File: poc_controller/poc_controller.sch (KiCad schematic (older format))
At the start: 8 parts, among them J1 CONN_01X02, J2 CONN_01X06, U1 MIC5211, U2 dspic33EP128GP502, U3 dspic33EP128GP502, U4 MPC8025

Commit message: Schematic updates for POC controller.
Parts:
- removed U2, U3: dspic33EP128GP502, symbol dspic33EP128GP502
- added C3, C4, C5: 0.1uF, symbol C
- added C6: 10uF, symbol C
- added C? (x2): C, symbol C
- added C? (x5): 100nF, symbol CP1
- added C?: 1uF, symbol CP1
- added C?: CP1, symbol CP1
- added J?: CONN_01X06, symbol CONN_01X06
- added J? (x2): CONN_01X02, symbol CONN_01X02
- added R1: 47k, symbol R
- added R?: R, symbol R
- added R? (x3): 4.7k, symbol R
- added U? (x2): dsPIC33EPXXXMC502, symbol dsPIC33EPXXXMC502
- added U?: MAG3110, symbol MAG3110
- added U?: LSM6DS3H, symbol LSM6DS3H
- added Y1: Crystal, symbol Crystal
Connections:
- net labels added: CAN_RX, CAN_TX, CPU_MCLR, CPU_PGC, CPU_PGD, SCL, SDA
- wire segments 29 -> 98
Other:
- moved on the sheet: C1, C2

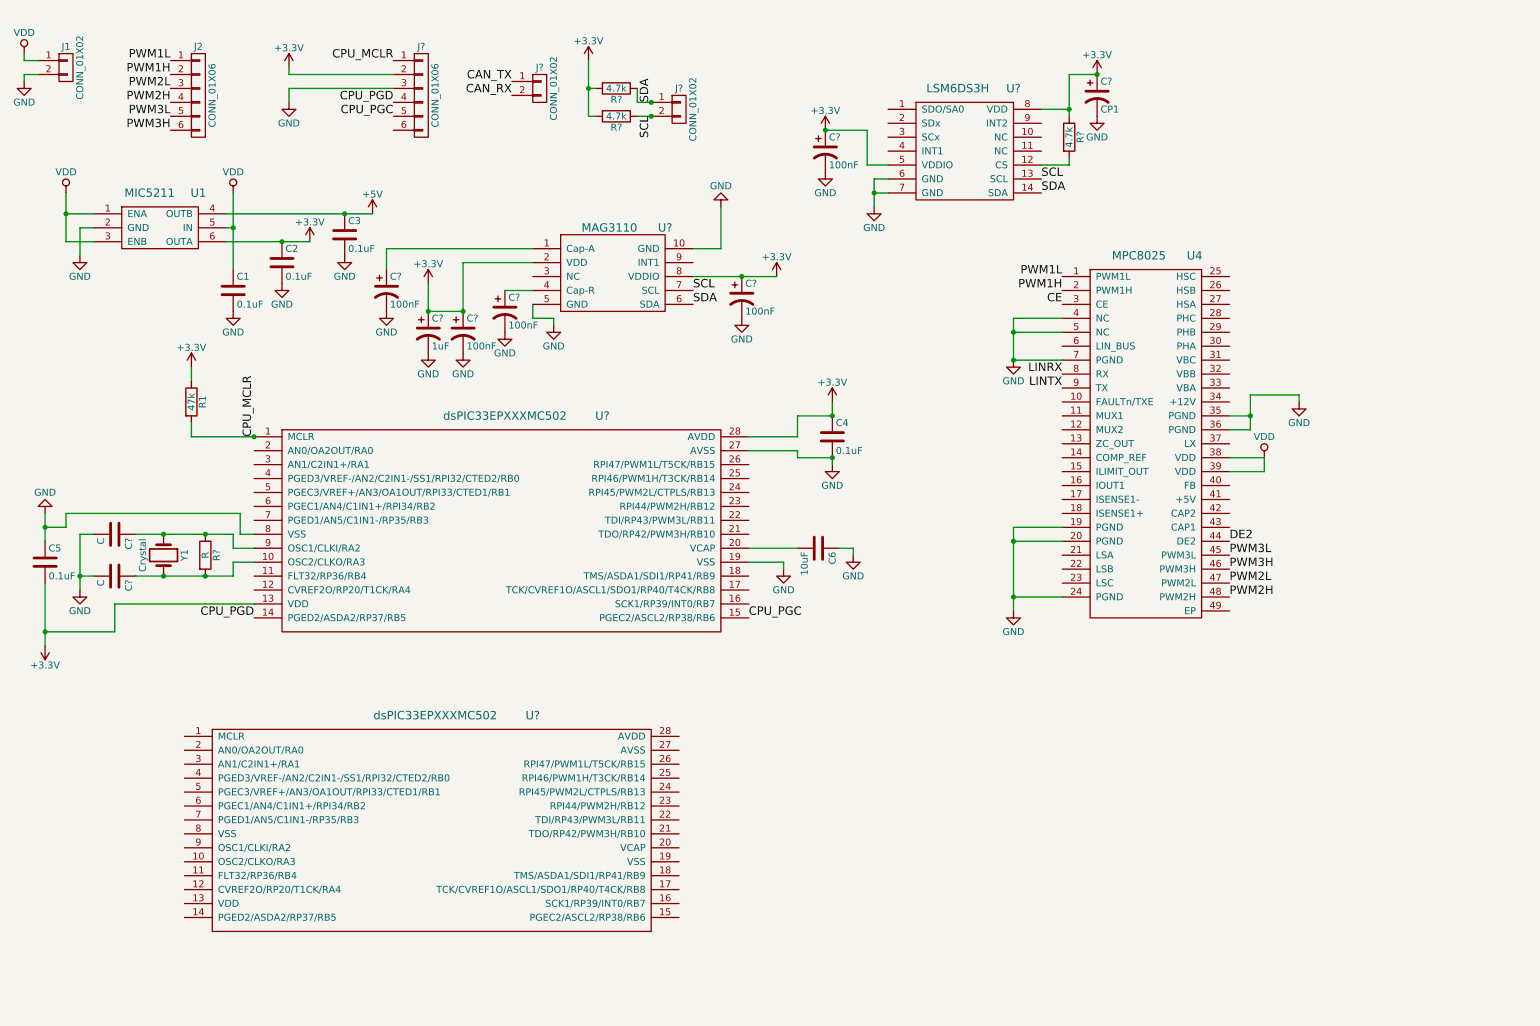
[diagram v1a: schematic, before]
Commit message: Start to break out sections into separate sheets.
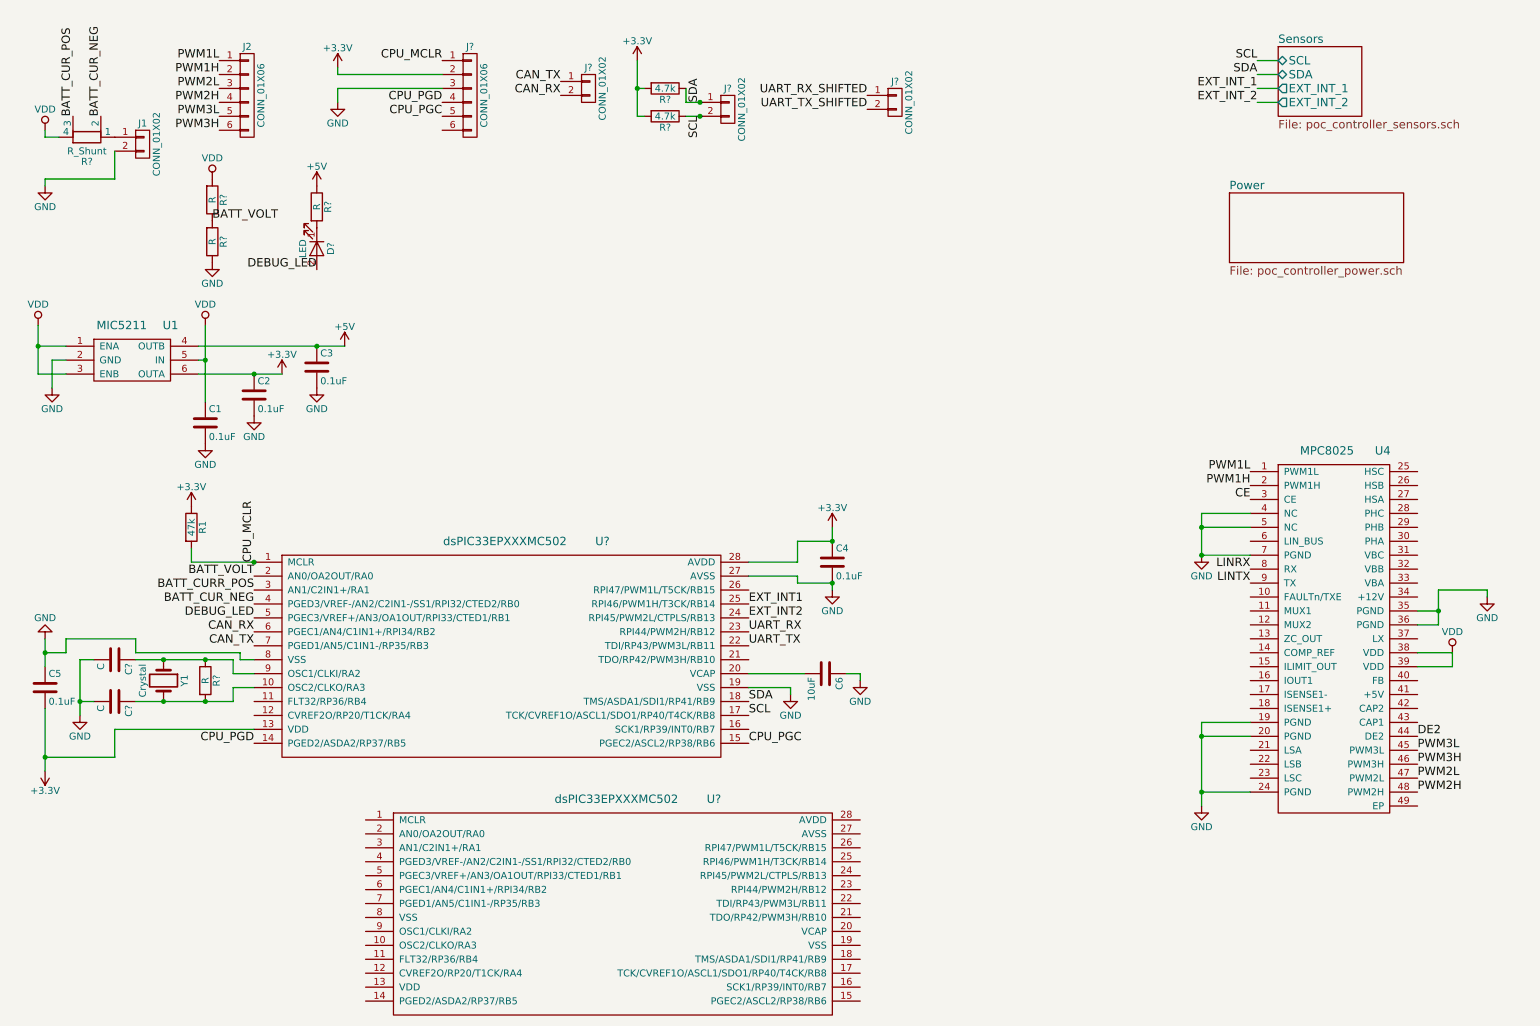
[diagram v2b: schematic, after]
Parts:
- removed C? (x5): 100nF, symbol CP1
- removed C?: 1uF, symbol CP1
- removed C?: CP1, symbol CP1
- removed R?: 4.7k, symbol R
- removed U?: MAG3110, symbol MAG3110
- removed U?: LSM6DS3H, symbol LSM6DS3H
- added D?: LED, symbol LED
- added J?: CONN_01X02, symbol CONN_01X02
- added R?: R_Shunt, symbol R_Shunt
- added R? (x3): R, symbol R
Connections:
- net +5V: now also R?.1
- net CAN_RX: now also U?.6 (PGEC1/AN4/C1IN1+/RPI34/RB2)
- net CAN_TX: now also U?.7 (PGED1/AN5/C1IN1-/RP35/RB3)
- net GND: now also R?.1
- net SCL: now also U?.17 (TCK/CVREF1O/ASCL1/SDO1/RP40/T4CK/RB8)
- net SDA: now also U?.18 (TMS/ASDA1/SDI1/RP41/RB9)
- net VDD: now also R?.2, R?.4; no longer J1.1 (P1)
- net BATT_VOLT: now reaches U?.2 (AN0/OA2OUT/RA0)
- net BATT_VOLT: now also R?.1, R?.2
- net UART_TX: now reaches U?.22 (TDI/RP43/PWM3L/RB11)
- net UART_RX: now reaches U?.23 (RPI44/PWM2H/RB12)
- net EXT_INT2: now reaches U?.24 (RPI45/PWM2L/CTPLS/RB13)
- net EXT_INT1: now reaches U?.25 (RPI46/PWM1H/T3CK/RB14)
- net BATT_CURR_POS: now reaches U?.3 (AN1/C2IN1+/RA1)
- net BATT_CUR_NEG: now reaches U?.4 (PGED3/VREF-/AN2/C2IN1-/SS1/RPI32/CTED2/RB0)
- net BATT_CUR_NEG: now also R?.2
- net DEBUG_LED: now reaches U?.5 (PGEC3/VREF+/AN3/OA1OUT/RPI33/CTED1/RB1)
- net DEBUG_LED: now also D?.2 (A)
- new net: J1.1 (P1), R?.1
- new net: D?.1 (K), R?.2
- new net BATT_CUR_POS: R?.3
- new net UART_RX_SHIFTED: J?.1 (P1)
- new net UART_TX_SHIFTED: J?.2 (P2)
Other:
- moved on the sheet: C1, C2, C3, C4, C5, C6, C?, J1, J2, J?, R1, R?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

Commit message: WIP
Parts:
- removed C1, C2, C3: 0.1uF, symbol C
- removed J1: CONN_01X02, symbol CONN_01X02
- removed R?: R_Shunt, symbol R_Shunt
- removed R? (x2): R, symbol R
- removed U1: MIC5211, symbol MIC5211

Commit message: Start assigning footprints and cleaning things up.
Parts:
- C2: renamed from C?; footprint (none) -> Capacitors_SMD:CP_Elec_3x5.3
- J1: renamed from J2; footprint (none) -> Pin_Headers:Pin_Header_Straight_1x06_Pitch2.54mm
- J2: renamed from J?; footprint (none) -> Pin_Headers:Pin_Header_Straight_1x06_Pitch2.54mm
- J3, J4, J5: renamed from J?; footprint (none) -> Pin_Headers:Pin_Header_Straight_1x02_Pitch2.54mm
- gave numbers to parts that had none: 8
- renumbered C5 to C1, C6 to C4, C4 to C5, U4 to U3
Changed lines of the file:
@@
 $Descr A4 11693 8268
 encoding utf-8
-Sheet 1 3
+Sheet 1 4
 Title ""
 Date ""
@@
 $EndDescr
 $Comp
-L MPC8025 U4
+L MPC8025 U3
 U 1 1 597DE643
 P 9950 3550
-F 0 "U4" H 10350 3550 60  0000 C CNN
+F 0 "U3" H 10350 3550 60  0000 C CNN
 F 1 "MPC8025" H 9950 3550 60  0000 C CNN
 F 2 "" H 9950 3550 60  0001 C CNN
@@
 $EndComp
 $Comp
-L VDD #PWR?
+L VDD #PWR15
 U 1 1 597F7D5C
 P 10850 5000
-F 0 "#PWR?" H 10850 4850 50  0001 C CNN
+F 0 "#PWR15" H 10850 4850 50  0001 C CNN
 F 1 "VDD" H 10850 5150 50  0000 C CNN
 F 2 "" H 10850 5000 50  0001 C CNN
@@
 $EndComp
 $Comp
-L GND #PWR?
+L GND #PWR13
 U 1 1 597F7DBF
 P 9050 4300
-F 0 "#PWR?" H 9050 4050 50  0001 C CNN
+F 0 "#PWR13" H 9050 4050 50  0001 C CNN
 F 1 "GND" H 9050 4150 50  0000 C CNN
 F 2 "" H 9050 4300 50  0001 C CNN
@@
 $EndComp
 $Comp
-L GND #PWR?
+L GND #PWR14
 U 1 1 597F7E00
 P 9050 6100
-F 0 "#PWR?" H 9050 5850 50  0001 C CNN
+F 0 "#PWR14" H 9050 5850 50  0001 C CNN
 F 1 "GND" H 9050 5950 50  0000 C CNN
 F 2 "" H 9050 6100 50  0001 C CNN
@@
 $EndComp
 $Comp
-L GND #PWR?
+L GND #PWR16
 U 1 1 597F7E46
 P 11100 4600
-F 0 "#PWR?" H 11100 4350 50  0001 C CNN
+F 0 "#PWR16" H 11100 4350 50  0001 C CNN
 F 1 "GND" H 11100 4450 50  0000 C CNN
 F 2 "" H 11100 4600 50  0001 C CNN
@@
 $EndComp
 $Comp
-L CONN_01X06 J2
+L CONN_01X06 J1
 U 1 1 597F7F2B
 P 2200 1000
-F 0 "J2" H 2200 1350 50  0000 C CNN
+F 0 "J1" H 2200 1350 50  0000 C CNN
 F 1 "CONN_01X06" V 2300 1000 50  0000 C CNN
-F 2 "" H 2200 1000 50  0001 C CNN
+F 2 "Pin_Headers:Pin_Header_Straight_1x06_Pitch2.54mm" H 2200 1000 50  0001 C CNN
 F 3 "" H 2200 1000 50  0001 C CNN
 	1    2200 1000
@@
 Connection ~ 9050 4300
 $Comp
-L dsPIC33EPXXXMC502 U?
+L dsPIC33EPXXXMC502 U1
 U 1 1 5988BD62
 P 4050 4200
-F 0 "U?" H 4750 4200 60  0000 C CNN
+F 0 "U1" H 4750 4200 60  0000 C CNN
 F 1 "dsPIC33EPXXXMC502" H 4050 4200 60  0000 C CNN
 F 2 "" H 4050 4200 60  0001 C CNN
@@
 $EndComp
 $Comp
-L dsPIC33EPXXXMC502 U?
+L dsPIC33EPXXXMC502 U2
 U 1 1 5988BDC3
 P 4850 6050
-F 0 "U?" H 5550 6050 60  0000 C CNN
+F 0 "U2" H 5550 6050 60  0000 C CNN
 F 1 "dsPIC33EPXXXMC502" H 4850 6050 60  0000 C CNN
 F 2 "" H 4850 6050 60  0001 C CNN
@@
 $EndComp
 $Comp
-L C C4
+L C C5
 U 1 1 5988BED8
 P 6400 4350
-F 0 "C4" H 6425 4450 50  0000 L CNN
+F 0 "C5" H 6425 4450 50  0000 L CNN
 F 1 "0.1uF" H 6425 4250 50  0000 L CNN
 F 2 "" H 6438 4200 50  0001 C CNN
@@
 $EndComp
 $Comp
-L C C5
+L C C1
 U 1 1 5988BF3B
 P 750 5250
-F 0 "C5" H 775 5350 50  0000 L CNN
+F 0 "C1" H 775 5350 50  0000 L CNN
 F 1 "0.1uF" H 775 5150 50  0000 L CNN
 F 2 "" H 788 5100 50  0001 C CNN
@@
 	6150 4200 6400 4200
 $Comp
-L GND #PWR?
+L GND #PWR11
 U 1 1 5988C24A
 P 6400 4550
-F 0 "#PWR?" H 6400 4300 50  0001 C CNN
+F 0 "#PWR11" H 6400 4300 50  0001 C CNN
 F 1 "GND" H 6400 4400 50  0000 C CNN
 F 2 "" H 6400 4550 50  0001 C CNN
@@
 	6400 4500 6400 4550
 $Comp
-L +3.3V #PWR?
+L +3.3V #PWR10
 U 1 1 5988C2BA
 P 6400 4100
-F 0 "#PWR?" H 6400 3950 50  0001 C CNN
+F 0 "#PWR10" H 6400 3950 50  0001 C CNN
 F 1 "+3.3V" H 6400 4240 50  0000 C CNN
 F 2 "" H 6400 4100 50  0001 C CNN
@@
 	750  5400 750  5850
 $Comp
-L GND #PWR?
+L GND #PWR1
 U 1 1 5988C4C9
 P 750 4900
-F 0 "#PWR?" H 750 4650 50  0001 C CNN
+F 0 "#PWR1" H 750 4650 50  0001 C CNN
 F 1 "GND" H 750 4750 50  0000 C CNN
 F 2 "" H 750 4900 50  0001 C CNN
@@
 $EndComp
 $Comp
-L +3.3V #PWR?
+L +3.3V #PWR2
 U 1 1 5988C5A5
 P 750 5850
-F 0 "#PWR?" H 750 5700 50  0001 C CNN
+F 0 "#PWR2" H 750 5700 50  0001 C CNN
 F 1 "+3.3V" H 750 5990 50  0000 C CNN
 F 2 "" H 750 5850 50  0001 C CNN
@@
 $EndComp
 $Comp
-L C C6
+L C C4
 U 1 1 5988C66D
 P 6350 5150
-F 0 "C6" H 6375 5250 50  0000 L CNN
+F 0 "C4" H 6375 5250 50  0000 L CNN
 F 1 "10uF" H 6375 5050 50  0000 L CNN
 F 2 "" H 6388 5000 50  0001 C CNN
@@
 $EndComp
 $Comp
-L GND #PWR?
+L GND #PWR12
 U 1 1 5988C761
 P 6600 5200
-F 0 "#PWR?" H 6600 4950 50  0001 C CNN
+F 0 "#PWR12" H 6600 4950 50  0001 C CNN
 F 1 "GND" H 6600 5050 50  0000 C CNN
 F 2 "" H 6600 5200 50  0001 C CNN
@@
 $EndComp
 $Comp
-L GND #PWR?
+L GND #PWR9
 U 1 1 5988C799
 P 6100 5300
-F 0 "#PWR?" H 6100 5050 50  0001 C CNN
+F 0 "#PWR9" H 6100 5050 50  0001 C CNN
 F 1 "GND" H 6100 5150 50  0000 C CNN
 F 2 "" H 6100 5300 50  0001 C CNN
@@
 	6600 5150 6600 5200
 $Comp
-L CONN_01X06 J?
+L CONN_01X06 J2
 U 1 1 5988CADA
 P 3800 1000
-F 0 "J?" H 3800 1350 50  0000 C CNN
+F 0 "J2" H 3800 1350 50  0000 C CNN
 F 1 "CONN_01X06" V 3900 1000 50  0000 C CNN
-F 2 "" H 3800 1000 50  0001 C CNN
+F 2 "Pin_Headers:Pin_Header_Straight_1x06_Pitch2.54mm" H 3800 1000 50  0001 C CNN
 F 3 "" H 3800 1000 50  0001 C CNN
 	1    3800 1000
@@
 CPU_PGC
 $Comp
-L +3.3V #PWR?
+L +3.3V #PWR6
 U 1 1 5988CBFB
 P 2850 800
-F 0 "#PWR?" H 2850 650 50  0001 C CNN
+F 0 "#PWR6" H 2850 650 50  0001 C CNN
 F 1 "+3.3V" H 2850 940 50  0000 C CNN
 F 2 "" H 2850 800 50  0001 C CNN
@@
 $EndComp
 $Comp
-L GND #PWR?
+L GND #PWR7
 U 1 1 5988CC36
 P 2850 1050
-F 0 "#PWR?" H 2850 800 50  0001 C CNN
+F 0 "#PWR7" H 2850 800 50  0001 C CNN
 F 1 "GND" H 2850 900 50  0000 C CNN
 F 2 "" H 2850 1050 50  0001 C CNN
@@
 	1800 4350 2250 4350
 $Comp
-L +3.3V #PWR?
+L +3.3V #PWR4
 U 1 1 5988CFE9
 P 1800 3950
-F 0 "#PWR?" H 1800 3800 50  0001 C CNN
+F 0 "#PWR4" H 1800 3800 50  0001 C CNN
 F 1 "+3.3V" H 1800 4090 50  0000 C CNN
 F 2 "" H 1800 3950 50  0001 C CNN
@@
 $EndComp
 $Comp
-L R R?
+L R R2
 U 1 1 59A8012A
 P 1900 5200
-F 0 "R?" V 1980 5200 50  0000 C CNN
+F 0 "R2" V 1980 5200 50  0000 C CNN
 F 1 "R" V 1900 5200 50  0000 C CNN
 F 2 "" V 1830 5200 50  0001 C CNN
@@
 $EndComp
 $Comp
-L C C?
+L C C2
 U 1 1 59A803A7
 P 1250 5050
-F 0 "C?" H 1275 5150 50  0000 L CNN
+F 0 "C2" H 1275 5150 50  0000 L CNN
 F 1 "C" H 1275 4950 50  0000 L CNN
-F 2 "" H 1288 4900 50  0001 C CNN
+F 2 "Capacitors_SMD:CP_Elec_3x5.3" H 1288 4900 50  0001 C CNN
 F 3 "" H 1250 5050 50  0001 C CNN
 	1    1250 5050
@@
 $EndComp
 $Comp
-L C C?
+L C C3
 U 1 1 59A80400
 P 1250 5350
-F 0 "C?" H 1275 5450 50  0000 L CNN
+F 0 "C3" H 1275 5450 50  0000 L CNN
 F 1 "C" H 1275 5250 50  0000 L CNN
 F 2 "" H 1288 5200 50  0001 C CNN
@@
 Connection ~ 1600 5050
 $Comp
-L GND #PWR?
+L GND #PWR3
 U 1 1 59A80A3B
 P 1000 5450
-F 0 "#PWR?" H 1000 5200 50  0001 C CNN
+F 0 "#PWR3" H 1000 5200 50  0001 C CNN
 F 1 "GND" H 1000 5300 50  0000 C CNN
 F 2 "" H 1000 5450 50  0001 C CNN
@@
 Connection ~ 750  5750
 $Comp
-L CONN_01X02 J?
+L CONN_01X02 J3
 U 1 1 59A81295
 P 4650 950
-F 0 "J?" H 4650 1100 50  0000 C CNN
+F 0 "J3" H 4650 1100 50  0000 C CNN
 F 1 "CONN_01X02" V 4750 950 50  0000 C CNN
-F 2 "" H 4650 950 50  0001 C CNN
+F 2 "Pin_Headers:Pin_Header_Straight_1x02_Pitch2.54mm" H 4650 950 50  0001 C CNN
 F 3 "" H 4650 950 50  0001 C CNN
 	1    4650 950
@@
 CAN_RX
 $Comp
-L CONN_01X02 J?
+L CONN_01X02 J4
 U 1 1 59A839DB
 P 5650 1100
-F 0 "J?" H 5650 1250 50  0000 C CNN
+F 0 "J4" H 5650 1250 50  0000 C CNN
 F 1 "CONN_01X02" V 5750 1100 50  0000 C CNN
-F 2 "" H 5650 1100 50  0001 C CNN
+F 2 "Pin_Headers:Pin_Header_Straight_1x02_Pitch2.54mm" H 5650 1100 50  0001 C CNN
 F 3 "" H 5650 1100 50  0001 C CNN
 	1    5650 1100
@@
 $EndComp
 $Comp
-L R R?
+L R R4
 U 1 1 59A83A62
 P 5200 950
-F 0 "R?" V 5280 950 50  0000 C CNN
+F 0 "R4" V 5280 950 50  0000 C CNN
 F 1 "4.7k" V 5200 950 50  0000 C CNN
 F 2 "" V 5130 950 50  0001 C CNN
@@
 $EndComp
 $Comp
-L R R?
+L R R5
 U 1 1 59A83AD8
 P 5200 1150
-F 0 "R?" V 5280 1150 50  0000 C CNN
+F 0 "R5" V 5280 1150 50  0000 C CNN
 F 1 "4.7k" V 5200 1150 50  0000 C CNN
 F 2 "" V 5130 1150 50  0001 C CNN
@@
 $EndComp
 $Comp
-L +3.3V #PWR?
+L +3.3V #PWR8
 U 1 1 59A83B4F
 P 5000 750
-F 0 "#PWR?" H 5000 600 50  0001 C CNN
+F 0 "#PWR8" H 5000 600 50  0001 C CNN
 F 1 "+3.3V" H 5000 890 50  0000 C CNN
 F 2 "" H 5000 750 50  0001 C CNN
@@
 BATT_CUR_NEG
 $Comp
-L +5V #PWR?
+L +5V #PWR5
 U 1 1 5A0112ED
 P 2700 1650
-F 0 "#PWR?" H 2700 1500 50  0001 C CNN
+F 0 "#PWR5" H 2700 1500 50  0001 C CNN
 F 1 "+5V" H 2700 1790 50  0000 C CNN
 F 2 "" H 2700 1650 50  0001 C CNN
@@
 $EndComp
 $Comp
-L R R?
+L R R3
 U 1 1 5A01136A
 P 2700 1800
-F 0 "R?" V 2780 1800 50  0000 C CNN
+F 0 "R3" V 2780 1800 50  0000 C CNN
 F 1 "R" V 2700 1800 50  0000 C CNN
 F 2 "" V 2630 1800 50  0001 C CNN
@@
 $EndComp
 $Comp
-L LED D?
+L LED D1
 U 1 1 5A011403
 P 2700 2100
-F 0 "D?" H 2700 2200 50  0000 C CNN
+F 0 "D1" H 2700 2200 50  0000 C CNN
 F 1 "LED" H 2700 2000 50  0000 C CNN
 F 2 "" H 2700 2100 50  0001 C CNN
@@
 DEBUG_LED
 $Comp
-L CONN_01X02 J?
+L CONN_01X02 J5
 U 1 1 5A011CCC
 P 6850 1050
-F 0 "J?" H 6850 1200 50  0000 C CNN
+F 0 "J5" H 6850 1200 50  0000 C CNN
 F 1 "CONN_01X02" V 6950 1050 50  0000 C CNN
-F 2 "" H 6850 1050 50  0001 C CNN
+F 2 "Pin_Headers:Pin_Header_Straight_1x02_Pitch2.54mm" H 6850 1050 50  0001 C CNN
 F 3 "" H 6850 1050 50  0001 C CNN
 	1    6850 1050
@@
 Wire Wire Line
 	9400 1750 9600 1750
+$Sheet
+S 9600 2150 500  150
+U 5A10B6B3
+F0 "Motor" 60
+F1 "poc_controller_motor.sch" 60
+$EndSheet
 $EndSCHEMATC

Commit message: More design and component selection.
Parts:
- removed U2: dsPIC33EPXXXMC502, symbol dsPIC33EPXXXMC502
- removed U3: MPC8025, symbol MPC8025
- added SW1: SW_DPST, Buttons_Switches_SMD:SW_SPST_B3SL-1022P, symbol SW_DPST
- Y1: footprint (none) -> Crystals:Crystal_SMD_HC49-SD_HandSoldering
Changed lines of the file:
@@
 LIBS:valves
 LIBS:quadcopter_lib
+LIBS:switches
 LIBS:poc_controller-cache
 EELAYER 25 0
@@
 $EndDescr
 $Comp
-L MPC8025 U3
-U 1 1 597DE643
-P 9950 3550
-F 0 "U3" H 10350 3550 60  0000 C CNN
-F 1 "MPC8025" H 9950 3550 60  0000 C CNN
-F 2 "" H 9950 3550 60  0001 C CNN
-F 3 "" H 9950 3550 60  0001 C CNN
-	1    9950 3550
-	1    0    0    -1
-$EndComp
-$Comp
-L VDD #PWR15
-U 1 1 597F7D5C
-P 10850 5000
-F 0 "#PWR15" H 10850 4850 50  0001 C CNN
-F 1 "VDD" H 10850 5150 50  0000 C CNN
-F 2 "" H 10850 5000 50  0001 C CNN
-F 3 "" H 10850 5000 50  0001 C CNN
-	1    10850 5000
-	1    0    0    -1
-$EndComp
-$Comp
-L GND #PWR13
-U 1 1 597F7DBF
-P 9050 4300
-F 0 "#PWR13" H 9050 4050 50  0001 C CNN
-F 1 "GND" H 9050 4150 50  0000 C CNN
-F 2 "" H 9050 4300 50  0001 C CNN
-F 3 "" H 9050 4300 50  0001 C CNN
-	1    9050 4300
-	1    0    0    -1
-$EndComp
-$Comp
-L GND #PWR14
-U 1 1 597F7E00
-P 9050 6100
-F 0 "#PWR14" H 9050 5850 50  0001 C CNN
-F 1 "GND" H 9050 5950 50  0000 C CNN
-F 2 "" H 9050 6100 50  0001 C CNN
-F 3 "" H 9050 6100 50  0001 C CNN
-	1    9050 6100
-	1    0    0    -1
-$EndComp
-$Comp
-L GND #PWR16
-U 1 1 597F7E46
-P 11100 4600
-F 0 "#PWR16" H 11100 4350 50  0001 C CNN
-F 1 "GND" H 11100 4450 50  0000 C CNN
-F 2 "" H 11100 4600 50  0001 C CNN
-F 3 "" H 11100 4600 50  0001 C CNN
-	1    11100 4600
-	1    0    0    -1
-$EndComp
-$Comp
 L CONN_01X06 J1
 U 1 1 597F7F2B
@@
 	1    0    0    -1
 $EndComp
-Text Label 9400 3700 2    60   ~ 0
-PWM1L
-Text Label 9400 3800 2    60   ~ 0
-PWM1H
 Text Label 2000 750  2    60   ~ 0
 PWM1L
@@
 Text Label 2000 1250 2    60   ~ 0
 PWM3H
-Text Label 10600 5700 0    60   ~ 0
-PWM3L
-Text Label 10600 5800 0    60   ~ 0
-PWM3H
-Text Label 10600 5900 0    60   ~ 0
-PWM2L
-Text Label 10600 6000 0    60   ~ 0
-PWM2H
-Text Label 9400 3900 2    60   ~ 0
-CE
-Text Label 9400 4400 2    60   ~ 0
-LINRX
-Text Label 9400 4500 2    60   ~ 0
-LINTX
-Text Label 10600 5600 0    60   ~ 0
-DE2
-Wire Wire Line
-	10850 5000 10600 5000
-Wire Wire Line
-	10850 5000 10850 5100
-Wire Wire Line
-	10850 5100 10600 5100
-Wire Wire Line
-	9050 4300 9400 4300
-Wire Wire Line
-	9050 6000 9400 6000
-Wire Wire Line
-	9050 5500 9050 6100
-Wire Wire Line
-	9400 5600 9050 5600
-Connection ~ 9050 6000
-Wire Wire Line
-	9400 5500 9050 5500
-Connection ~ 9050 5600
-Wire Wire Line
-	10750 4800 10600 4800
-Wire Wire Line
-	10750 4550 10750 4800
-Wire Wire Line
-	10750 4550 11100 4550
-Wire Wire Line
-	11100 4550 11100 4600
-Wire Wire Line
-	10600 4700 10750 4700
-Connection ~ 10750 4700
-Wire Wire Line
-	9400 4100 9050 4100
-Wire Wire Line
-	9050 4000 9050 4300
-Wire Wire Line
-	9400 4000 9050 4000
-Connection ~ 9050 4100
-Connection ~ 9050 4300
 $Comp
 L dsPIC33EPXXXMC502 U1
@@
 F 3 "" H 4050 4200 60  0001 C CNN
 	1    4050 4200
-	1    0    0    -1
-$EndComp
-$Comp
-L dsPIC33EPXXXMC502 U2
-U 1 1 5988BDC3
-P 4850 6050
-F 0 "U2" H 5550 6050 60  0000 C CNN
-F 1 "dsPIC33EPXXXMC502" H 4850 6050 60  0000 C CNN
-F 2 "" H 4850 6050 60  0001 C CNN
-F 3 "" H 4850 6050 60  0001 C CNN
-	1    4850 6050
 	1    0    0    -1
 $EndComp
@@
 F 0 "Y1" H 1600 5350 50  0000 C CNN
 F 1 "Crystal" H 1600 5050 50  0000 C CNN
-F 2 "" H 1600 5200 50  0001 C CNN
+F 2 "Crystals:Crystal_SMD_HC49-SD_HandSoldering" H 1600 5200 50  0001 C CNN
 F 3 "" H 1600 5200 50  0001 C CNN
 	1    1600 5200
@@
 F1 "poc_controller_motor.sch" 60
 $EndSheet
+$Comp
+L SW_DPST SW1
+U 1 1 5AC186DD
+P 1050 3750
+F 0 "SW1" H 1050 3950 50  0000 C CNN
+F 1 "SW_DPST" H 1050 3550 50  0000 C CNN
+F 2 "Buttons_Switches_SMD:SW_SPST_B3SL-1022P" H 1050 3750 50  0001 C CNN
+F 3 "" H 1050 3750 50  0001 C CNN
+F 4 "SW1065CT-ND" H 1050 3750 60  0001 C CNN "Part Number"
+	1    1050 3750
+	1    0    0    -1
+$EndComp
 $EndSCHEMATC
